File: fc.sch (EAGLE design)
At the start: 72 parts, among them IC1 BN055, J1 USBC, U1 LMZ21700, U2 ATMEGA2560-16AU100A-M, U3 SI8621AB-B-IS, U4 FT230XQ, Y1 16MHz, Y2 32.768kHz

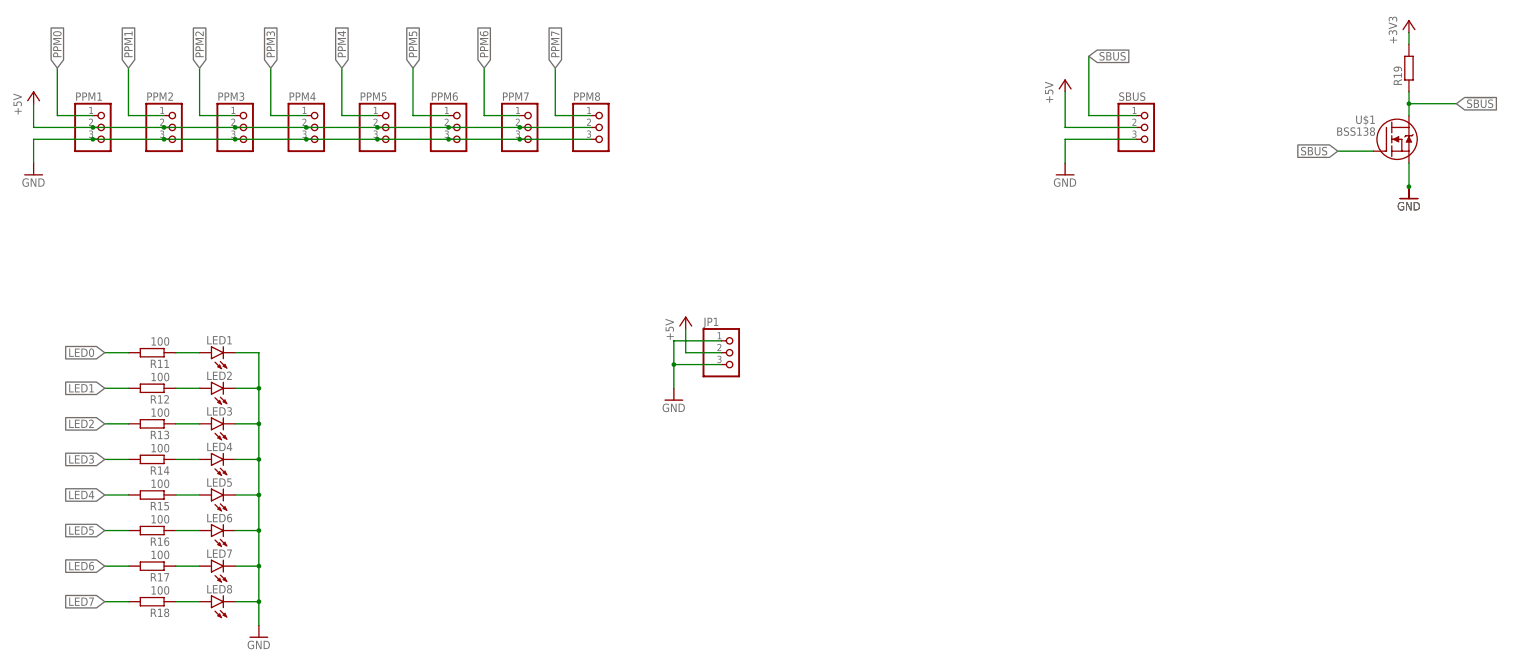
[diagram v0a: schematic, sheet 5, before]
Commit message: changed resistors to sparkfun lib
how nice, all the 0603 parts are the same size now.
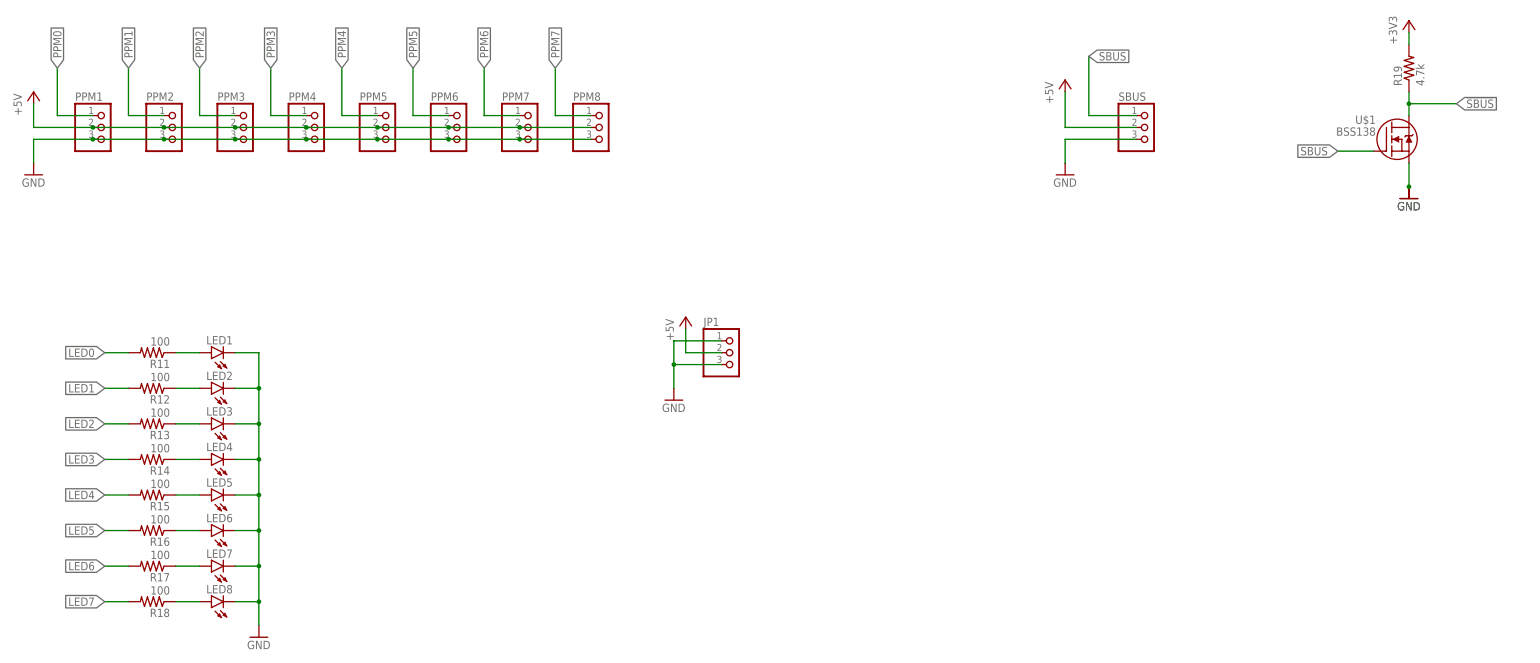
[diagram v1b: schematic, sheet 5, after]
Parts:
- R11, R12, R13, R14, R15, R16, R17, R18: device rcl:R-EU_R0603 -> SparkFun-Resistors:RESISTOR0603
- R19: value (none) -> 4.7k; device resistor:R-EU_R0603 -> SparkFun-Resistors:RESISTOR0603
- R3, R4: device resistor:R-EU_R0603 -> SparkFun-Resistors:RESISTOR0603
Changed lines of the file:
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@@
 <part name="+3V2" library="supply1" library_urn="urn:adsk.eagle:library:371" deviceset="+3V3" device=""/>
 <part name="GND8" library="supply1" library_urn="urn:adsk.eagle:library:371" deviceset="GND" device=""/>
-<part name="R4" library="resistor" library_urn="urn:adsk.eagle:library:348" deviceset="R-EU_" device="R0603" package3d_urn="urn:adsk.eagle:package:23555/2" value="10k"/>
+<part name="R4" library="SparkFun-Resistors" library_urn="urn:adsk.eagle:library:532" deviceset="RESISTOR" device="0603" package3d_urn="urn:adsk.eagle:package:39650/1" value="10k"/>
 <part name="+3V3" library="supply1" library_urn="urn:adsk.eagle:library:371" deviceset="+3V3" device=""/>
 <part name="GND9" library="supply1" library_urn="urn:adsk.eagle:library:371" deviceset="GND" device=""/>
@@
 <part name="U$1" library="hwp_SS18" deviceset="BSS138" device=""/>
 <part name="+3V5" library="supply1" library_urn="urn:adsk.eagle:library:371" deviceset="+3V3" device=""/>
-<part name="R19" library="resistor" library_urn="urn:adsk.eagle:library:348" deviceset="R-EU_" device="R0603" package3d_urn="urn:adsk.eagle:package:23555/2"/>
+<part name="R19" library="SparkFun-Resistors" library_urn="urn:adsk.eagle:library:532" deviceset="RESISTOR" device="0603" package3d_urn="urn:adsk.eagle:package:39650/1" value="4.7k"/>
 <part name="GND15" library="supply1" library_urn="urn:adsk.eagle:library:371" deviceset="GND" device=""/>
 <part name="GND16" library="supply1" library_urn="urn:adsk.eagle:library:371" deviceset="GND" device=""/>
-<part name="R11" library="rcl" library_urn="urn:adsk.eagle:library:334" deviceset="R-EU_" device="R0603" package3d_urn="urn:adsk.eagle:package:23555/2" value="100"/>
+<part name="R11" library="SparkFun-Resistors" library_urn="urn:adsk.eagle:library:532" deviceset="RESISTOR" device="0603" package3d_urn="urn:adsk.eagle:package:39650/1" value="100"/>
 <part name="LED1" library="SparkFun-LED" library_urn="urn:adsk.eagle:library:529" deviceset="LED" device="0603" package3d_urn="urn:adsk.eagle:package:39354/1"/>
 <part name="GND17" library="supply1" library_urn="urn:adsk.eagle:library:371" deviceset="GND" device=""/>
-<part name="R12" library="rcl" library_urn="urn:adsk.eagle:library:334" deviceset="R-EU_" device="R0603" package3d_urn="urn:adsk.eagle:package:23555/2" value="100"/>
+<part name="R12" library="SparkFun-Resistors" library_urn="urn:adsk.eagle:library:532" deviceset="RESISTOR" device="0603" package3d_urn="urn:adsk.eagle:package:39650/1" value="100"/>
 <part name="LED2" library="SparkFun-LED" library_urn="urn:adsk.eagle:library:529" deviceset="LED" device="0603" package3d_urn="urn:adsk.eagle:package:39354/1"/>
-<part name="R13" library="rcl" library_urn="urn:adsk.eagle:library:334" deviceset="R-EU_" device="R0603" package3d_urn="urn:adsk.eagle:package:23555/2" value="100"/>
+<part name="R13" library="SparkFun-Resistors" library_urn="urn:adsk.eagle:library:532" deviceset="RESISTOR" device="0603" package3d_urn="urn:adsk.eagle:package:39650/1" value="100"/>
 <part name="LED3" library="SparkFun-LED" library_urn="urn:adsk.eagle:library:529" deviceset="LED" device="0603" package3d_urn="urn:adsk.eagle:package:39354/1"/>
-<part name="R14" library="rcl" library_urn="urn:adsk.eagle:library:334" deviceset="R-EU_" device="R0603" package3d_urn="urn:adsk.eagle:package:23555/2" value="100"/>
+<part name="R14" library="SparkFun-Resistors" library_urn="urn:adsk.eagle:library:532" deviceset="RESISTOR" device="0603" package3d_urn="urn:adsk.eagle:package:39650/1" value="100"/>
 <part name="LED4" library="SparkFun-LED" library_urn="urn:adsk.eagle:library:529" deviceset="LED" device="0603" package3d_urn="urn:adsk.eagle:package:39354/1"/>
-<part name="R15" library="rcl" library_urn="urn:adsk.eagle:library:334" deviceset="R-EU_" device="R0603" package3d_urn="urn:adsk.eagle:package:23555/2" value="100"/>
+<part name="R15" library="SparkFun-Resistors" library_urn="urn:adsk.eagle:library:532" deviceset="RESISTOR" device="0603" package3d_urn="urn:adsk.eagle:package:39650/1" value="100"/>
 <part name="LED5" library="SparkFun-LED" library_urn="urn:adsk.eagle:library:529" deviceset="LED" device="0603" package3d_urn="urn:adsk.eagle:package:39354/1"/>
-<part name="R16" library="rcl" library_urn="urn:adsk.eagle:library:334" deviceset="R-EU_" device="R0603" package3d_urn="urn:adsk.eagle:package:23555/2" value="100"/>
+<part name="R16" library="SparkFun-Resistors" library_urn="urn:adsk.eagle:library:532" deviceset="RESISTOR" device="0603" package3d_urn="urn:adsk.eagle:package:39650/1" value="100"/>
 <part name="LED6" library="SparkFun-LED" library_urn="urn:adsk.eagle:library:529" deviceset="LED" device="0603" package3d_urn="urn:adsk.eagle:package:39354/1"/>
-<part name="R17" library="rcl" library_urn="urn:adsk.eagle:library:334" deviceset="R-EU_" device="R0603" package3d_urn="urn:adsk.eagle:package:23555/2" value="100"/>
+<part name="R17" library="SparkFun-Resistors" library_urn="urn:adsk.eagle:library:532" deviceset="RESISTOR" device="0603" package3d_urn="urn:adsk.eagle:package:39650/1" value="100"/>
 <part name="LED7" library="SparkFun-LED" library_urn="urn:adsk.eagle:library:529" deviceset="LED" device="0603" package3d_urn="urn:adsk.eagle:package:39354/1"/>
-<part name="R18" library="rcl" library_urn="urn:adsk.eagle:library:334" deviceset="R-EU_" device="R0603" package3d_urn="urn:adsk.eagle:package:23555/2" value="100"/>
+<part name="R18" library="SparkFun-Resistors" library_urn="urn:adsk.eagle:library:532" deviceset="RESISTOR" device="0603" package3d_urn="urn:adsk.eagle:package:39650/1" value="100"/>
 <part name="LED8" library="SparkFun-LED" library_urn="urn:adsk.eagle:library:529" deviceset="LED" device="0603" package3d_urn="urn:adsk.eagle:package:39354/1"/>
 <part name="JP1" library="pinhead" library_urn="urn:adsk.eagle:library:325" deviceset="PINHD-1X3" device="" package3d_urn="urn:adsk.eagle:package:22458/2"/>
@@
 <part name="GND26" library="supply1" library_urn="urn:adsk.eagle:library:371" deviceset="GND" device=""/>
 <part name="+3V8" library="supply1" library_urn="urn:adsk.eagle:library:371" deviceset="+3V3" device=""/>
-<part name="R3" library="resistor" library_urn="urn:adsk.eagle:library:348" deviceset="R-EU_" device="R0603" package3d_urn="urn:adsk.eagle:package:23555/2" value="10k"/>
+<part name="R3" library="SparkFun-Resistors" library_urn="urn:adsk.eagle:library:532" deviceset="RESISTOR" device="0603" package3d_urn="urn:adsk.eagle:package:39650/1" value="10k"/>
 <part name="S1" library="switch" deviceset="FSMSM" device=""/>
 <part name="U4" library="ftdichip" library_urn="urn:adsk.eagle:library:231" deviceset="FT230X" device="Q" package3d_urn="urn:adsk.eagle:package:14017/1"/>
